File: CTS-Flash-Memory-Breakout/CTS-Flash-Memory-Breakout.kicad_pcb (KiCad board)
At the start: 2 copper layers, 44.2 x 24 mm, 8 parts, among them J1 Conn_02x07_Counter_Clockwise, U1 S70FL01GSAGMFI011

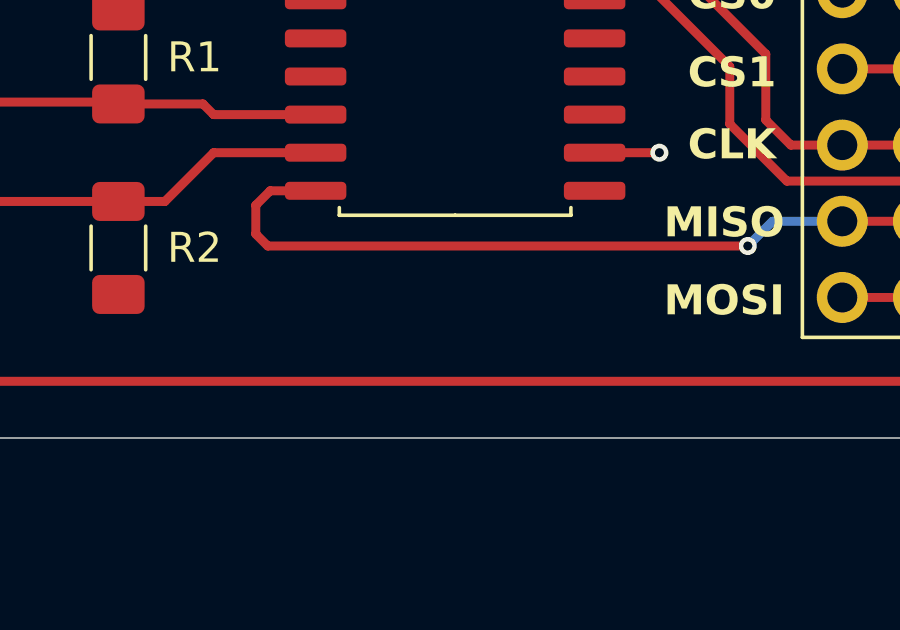
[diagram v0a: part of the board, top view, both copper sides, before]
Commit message: Silkscreen modifications
Added CTS logo to board alongside date and revision #
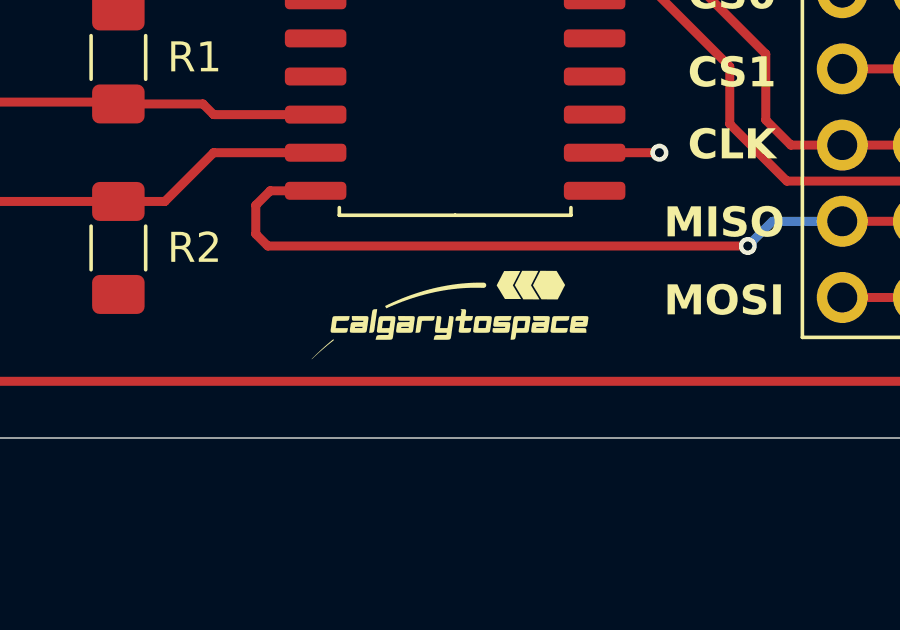
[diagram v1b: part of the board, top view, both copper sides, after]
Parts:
- added G***: LOGO, LOGO, F.Cu at (145.6, 90.4)
- added G***: LOGO, LOGO, B.Cu at (144.2, 90.6)
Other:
- board text added: "2024-05-27 Rev. 1"
